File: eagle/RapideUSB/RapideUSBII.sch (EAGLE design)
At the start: 58 parts, among them J1 AVR_SPI_PRG_6PTH, Q1 12MHz, Y1 12-20MHz

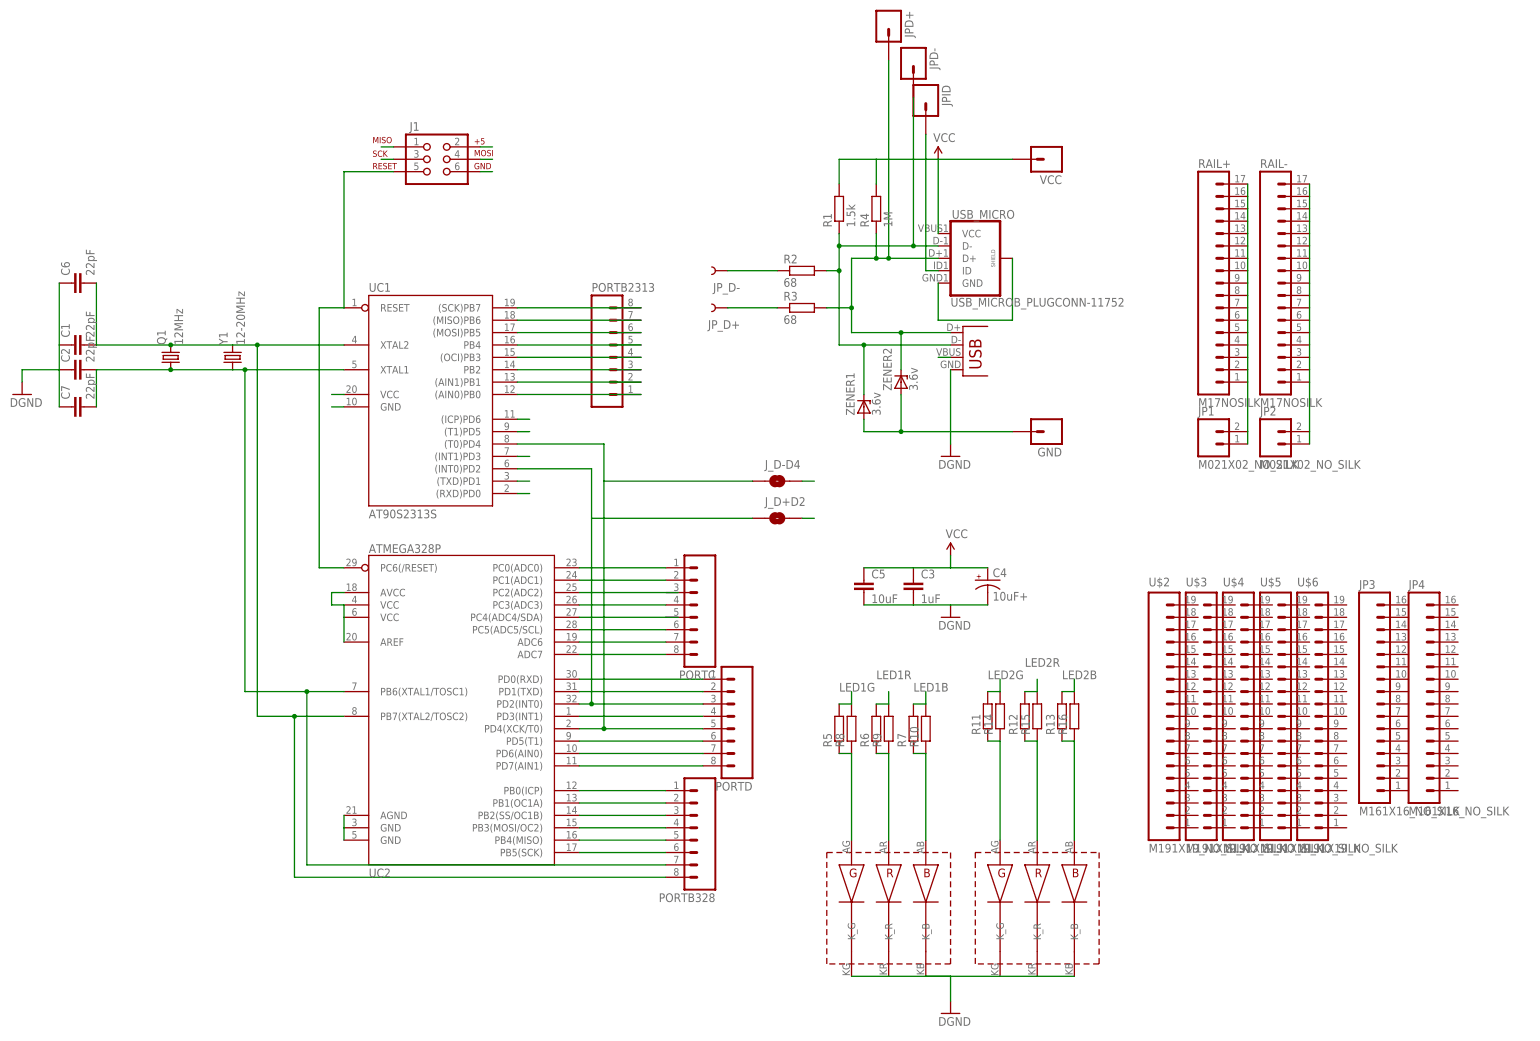
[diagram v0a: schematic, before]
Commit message: RapideUSBII : only 2313 before routing
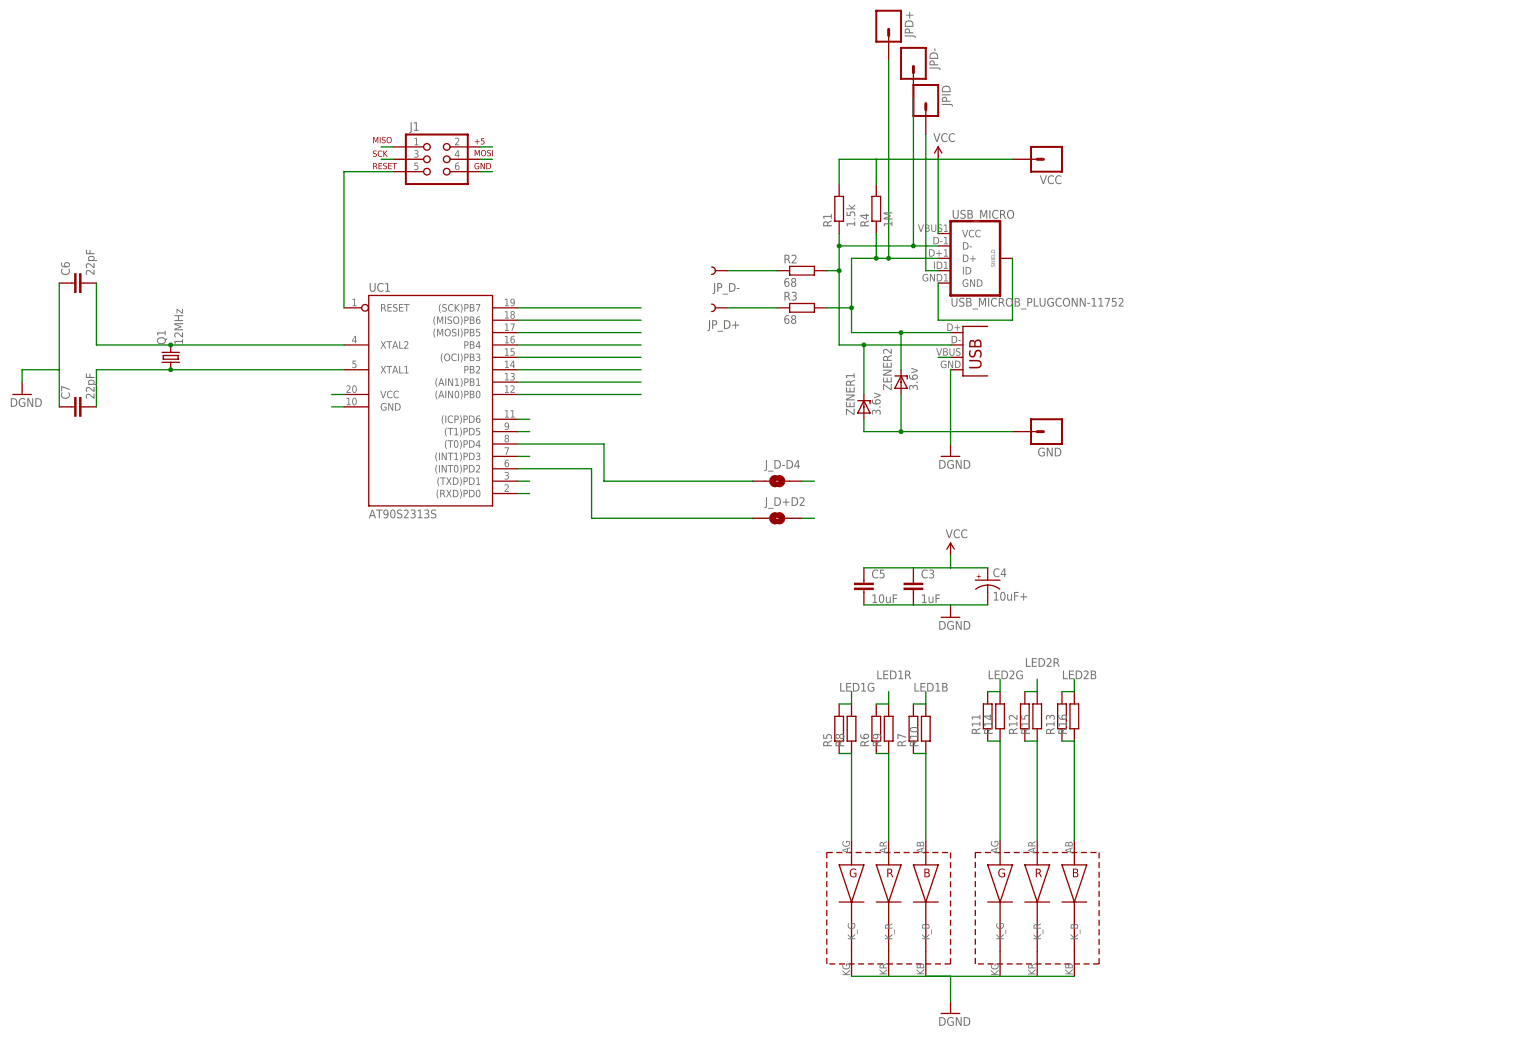
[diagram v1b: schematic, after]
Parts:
- removed C1, C2: 22pF, resistor:C-EU025-024X044
- removed JP1, JP2: M021X02_NO_SILK, SparkFun-Connectors:M021X02_NO_SILK
- removed JP3, JP4: M161X16_NO_SILK, SparkFun-Connectors:M161X16_NO_SILK
- removed PORTB2313, PORTB328, PORTC, PORTD: (no value), SparkFun-Connectors:M081X08
- removed RAIL+, RAIL-: M17NOSILK, SparkFun-Connectors:M17NOSILK
- removed U$2, U$3, U$4, U$5, U$6: M191X19_NO_SILK, SparkFun-Connectors:M191X19_NO_SILK
- removed UC2: ATMEGA328P, SparkFun-DigitalIC:ATMEGA328_SMT
- removed Y1: 12-20MHz, SparkFun-FreqCtrl:CRYSTALHC49UV
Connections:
- removed net B0: PORTB328.1, UC2.PB0(ICP)
- removed net B1: PORTB328.2, UC2.PB1(OC1A)
- removed net B2: PORTB328.3, UC2.PB2(SS/OC1B)
- removed net B6: C2.2, C7.2, PORTB328.7, Q1.1, UC1.XTAL1, UC2.PB6(XTAL1/TOSC1), Y1.1
- removed net B7: C1.2, C6.2, PORTB328.8, Q1.2, UC1.XTAL2, UC2.PB7(XTAL2/TOSC2), Y1.2
- removed net D7: PORTD.8, UC2.PD7(AIN1)
- removed net N$10: PORTC.6, UC2.PC5(ADC5/SCL)
- removed net N$11: PORTC.7, UC2.ADC6
- removed net N$12: PORTC.8, UC2.ADC7
- removed net N$16: PORTD.6, UC2.PD5(T1)
- removed net N$5: PORTC.1, UC2.PC0(ADC0)
- removed net N$6: PORTC.2, UC2.PC1(ADC1)
- removed net N$7: UC2.PC2(ADC2)
- removed net N$8: PORTC.4, UC2.PC3(ADC3)
- removed net N$9: PORTC.5, UC2.PC4(ADC4/SDA)
- new net N$22: C7.2, Q1.1, UC1.XTAL1
- new net N$23: C6.2, Q1.2, UC1.XTAL2
- net D0: no longer PORTD.1, UC2.PD0(RXD)
- net D1: no longer PORTD.2, UC2.PD1(TXD)
- net D2: no longer PORTD.3, UC2.PD2(INT0)
- net D3: no longer PORTD.4, UC2.PD3(INT1)
- net D4: no longer PORTD.5, UC2.PD4(XCK/T0)
- net D6: no longer PORTD.7, UC2.PD6(AIN0)
- net GND: no longer C1.1, C2.1, JP2.1, JP2.2, RAIL-.1, RAIL-.10, RAIL-.11, RAIL-.12, RAIL-.13, RAIL-.14, RAIL-.15, RAIL-.16, RAIL-.17, RAIL-.2, RAIL-.3, RAIL-.4, RAIL-.5, RAIL-.6, RAIL-.7, RAIL-.8, RAIL-.9, UC2.AGND, UC2.GND@1, UC2.GND@2
- net MISO: no longer PORTB2313.7, PORTB328.5, UC2.PB4(MISO)
- net MOSI: no longer PORTB2313.6, PORTB328.4, UC2.PB3(MOSI/OC2)
- net N$1: no longer PORTB2313.5
- net N$13: no longer PORTB2313.1
- net N$2: no longer PORTB2313.4
- net N$3: no longer PORTB2313.3
- net N$4: no longer PORTB2313.2
- net RESET: no longer UC2.PC6(/RESET)
- net SCK: no longer PORTB2313.8, PORTB328.6, UC2.PB5(SCK)
- net VCC: no longer JP1.1, JP1.2, RAIL+.1, RAIL+.10, RAIL+.11, RAIL+.12, RAIL+.13, RAIL+.14, RAIL+.15, RAIL+.16, RAIL+.17, RAIL+.2, RAIL+.3, RAIL+.4, RAIL+.5, RAIL+.6, RAIL+.7, RAIL+.8, RAIL+.9, UC2.AREF, UC2.AVCC, UC2.VCC@1, UC2.VCC@2

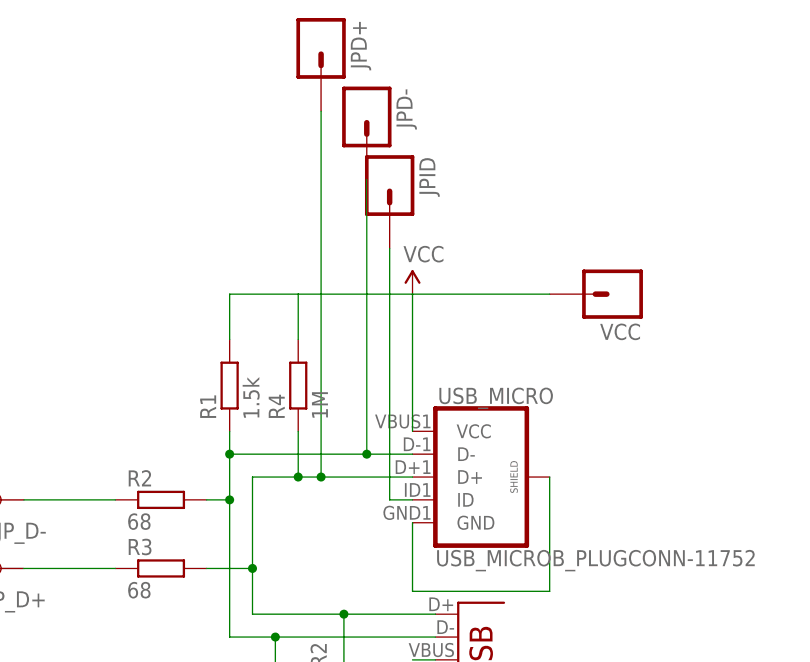
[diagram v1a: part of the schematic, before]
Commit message: Routed ok, need labelling
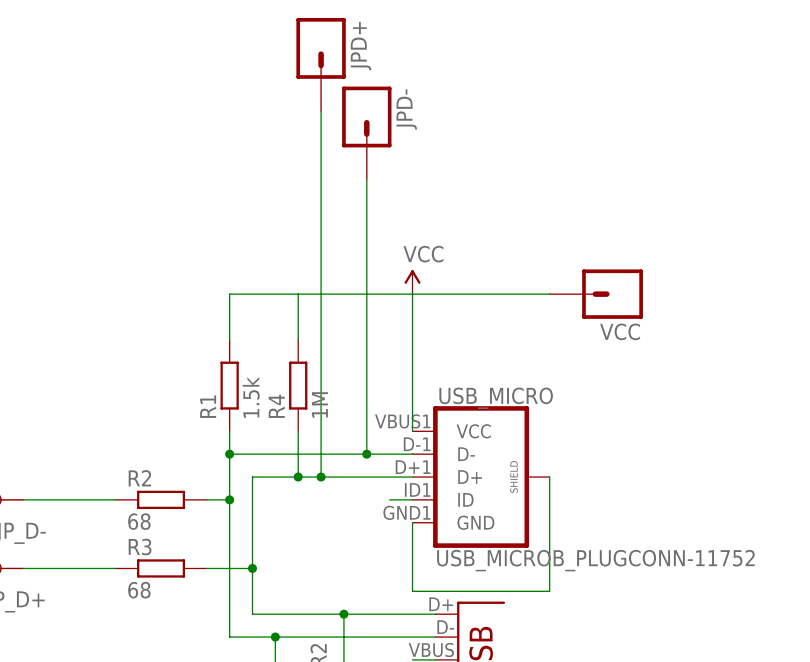
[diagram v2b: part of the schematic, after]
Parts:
- removed JPID: (no value), SparkFun-Connectors:M01PTH_NO_SILK_YES_STOP
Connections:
- removed net D5: UC1.(T1)PD5
- removed net D6: UC1.(ICP)PD6
- removed net N$13: UC1.(AIN0)PB0
- removed net N$2: UC1.(OCI)PB3
- removed net N$3: UC1.PB2
- removed net N$4: UC1.(AIN1)PB1
- net LED1B: now also UC1.(AIN0)PB0
- net LED1G: now also UC1.(ICP)PD6
- net LED1R: now also UC1.(T1)PD5
- net LED2B: now also UC1.(OCI)PB3
- net LED2G: now also UC1.PB2
- net LED2R: now also UC1.(AIN1)PB1
- net N$14: no longer JPID.1
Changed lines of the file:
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@@
 <part name="C7" library="SparkFun-Capacitors" deviceset="CAP" device="1206" value="22pF"/>
 <part name="Q1" library="crystal" deviceset="CRYSTAL" device="CTS406" value="12MHz"/>
-<part name="JPID" library="SparkFun-Connectors" deviceset="M01" device="PTH_NO_SILK_YES_STOP"/>
 <part name="LED1" library="kalshagar" deviceset="RGB-SMT-SQUARE" device="" technology="6X6MM"/>
 <part name="LED2" library="kalshagar" deviceset="RGB-SMT-SQUARE" device="5X5MM"/>
@@
 <instance part="C7" gate="G$1" x="-40.64" y="73.66" rot="R90"/>
 <instance part="Q1" gate="G$1" x="-22.86" y="83.82" rot="R90"/>
-<instance part="JPID" gate="G$1" x="132.08" y="137.16" rot="R270"/>
 <instance part="LED1" gate="G$1" x="124.46" y="-25.4"/>
 <instance part="LED2" gate="G$1" x="154.94" y="-25.4"/>
@@
 </segment>
 </net>
-<net name="D6" class="0">
-<segment>
-<pinref part="UC1" gate="G$1" pin="(ICP)PD6"/>
-<wire x1="48.26" y1="71.12" x2="50.8" y2="71.12" width="0.1524" layer="91"/>
-</segment>
-</net>
-<net name="D5" class="0">
-<segment>
-<pinref part="UC1" gate="G$1" pin="(T1)PD5"/>
-<wire x1="48.26" y1="68.58" x2="50.8" y2="68.58" width="0.1524" layer="91"/>
-</segment>
-</net>
 <net name="D3" class="0">
 <segment>
@@
 </segment>
 </net>
-<net name="N$2" class="0">
-<segment>
-<pinref part="UC1" gate="G$1" pin="(OCI)PB3"/>
-<wire x1="73.66" y1="83.82" x2="48.26" y2="83.82" width="0.1524" layer="91"/>
-</segment>
-</net>
-<net name="N$3" class="0">
-<segment>
-<pinref part="UC1" gate="G$1" pin="PB2"/>
-<wire x1="48.26" y1="81.28" x2="73.66" y2="81.28" width="0.1524" layer="91"/>
-</segment>
-</net>
-<net name="N$4" class="0">
-<segment>
-<pinref part="UC1" gate="G$1" pin="(AIN1)PB1"/>
-<wire x1="73.66" y1="78.74" x2="48.26" y2="78.74" width="0.1524" layer="91"/>
-</segment>
-</net>
-<net name="N$13" class="0">
-<segment>
-<pinref part="UC1" gate="G$1" pin="(AIN0)PB0"/>
-<wire x1="48.26" y1="76.2" x2="73.66" y2="76.2" width="0.1524" layer="91"/>
-</segment>
-</net>
 <net name="N$14" class="0">
 <segment>
-<pinref part="JPID" gate="G$1" pin="1"/>
-<wire x1="132.08" y1="129.54" x2="132.08" y2="101.6" width="0.1524" layer="91"/>
 <pinref part="USB_MICRO" gate="G$1" pin="ID"/>
 <wire x1="132.08" y1="101.6" x2="134.62" y2="101.6" width="0.1524" layer="91"/>
@@
 <label x="114.3" y="15.24" size="1.778" layer="95"/>
 </segment>
+<segment>
+<pinref part="UC1" gate="G$1" pin="(ICP)PD6"/>
+<wire x1="48.26" y1="71.12" x2="50.8" y2="71.12" width="0.1524" layer="91"/>
+</segment>
 </net>
 <net name="LED1R" class="0">
@@
 <label x="121.92" y="17.78" size="1.778" layer="95"/>
 </segment>
+<segment>
+<pinref part="UC1" gate="G$1" pin="(T1)PD5"/>
+<wire x1="48.26" y1="68.58" x2="50.8" y2="68.58" width="0.1524" layer="91"/>
+</segment>
 </net>
 <net name="LED1B" class="0">
@@
 <label x="129.54" y="15.24" size="1.778" layer="95"/>
 </segment>
+<segment>
+<pinref part="UC1" gate="G$1" pin="(AIN0)PB0"/>
+<wire x1="48.26" y1="76.2" x2="73.66" y2="76.2" width="0.1524" layer="91"/>
+</segment>
 </net>
 <net name="N$19" class="0">
@@
 <label x="144.78" y="17.78" size="1.778" layer="95"/>
 </segment>
+<segment>
+<pinref part="UC1" gate="G$1" pin="PB2"/>
+<wire x1="48.26" y1="81.28" x2="73.66" y2="81.28" width="0.1524" layer="91"/>
+</segment>
 </net>
 <net name="LED2R" class="0">
@@
 <label x="152.4" y="20.32" size="1.778" layer="95"/>
 </segment>
+<segment>
+<pinref part="UC1" gate="G$1" pin="(AIN1)PB1"/>
+<wire x1="73.66" y1="78.74" x2="48.26" y2="78.74" width="0.1524" layer="91"/>
+</segment>
 </net>
 <net name="LED2B" class="0">
@@
 <label x="160.02" y="17.78" size="1.778" layer="95"/>
 </segment>
-</net>
+<segment>
+<pinref part="UC1" gate="G$1" pin="(OCI)PB3"/>
+<wire x1="73.66" y1="83.82" x2="48.26" y2="83.82" width="0.1524" layer="91"/>
+</segment>
+</net>

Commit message: Before resuming working on RapiedUSBII, a quick commit of whatever I did.
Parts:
- added TP_ID: TEST-POINT3X5, SparkFun-Connectors:TEST-POINT3X5
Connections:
- net N$14: now also TP_ID.1

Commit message: Before routing
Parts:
- added H1: MOUNT-HOLE2.8, holes:MOUNT-HOLE2.8
- added J10: (no value), SparkFun-Connectors:CONN_08SMD-STRAIGHT-FEMALE
- added J2, J4, J5, J6, J7, J8: (no value), SparkFun-Connectors:CONN_08NO_SILK_FEMALE_PTH
- added J3: (no value), SparkFun-Connectors:CONN_08SMD-STRAIGHT-ALT-FEMALE
- added J9: (no value), SparkFun-Connectors:CONN_06NO_SILK_FEMALE_PTH
- Q1: device crystal:CRYSTALCTS406 -> SparkFun-Clocks:CRYSTALPTH-HC49UV
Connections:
- net D0: now also J10.8
- net D1: now also J10.7
- net D2: now also J10.6
- net D3: now also J10.5
- net D4: now also J10.4
- net GND: now also J9.1, J9.2, J9.3
- net LED1B: now also J3.8
- net LED1G: now also J10.2
- net LED1R: now also J10.3
- net LED2B: now also J3.5
- net LED2G: now also J3.6
- net LED2R: now also J3.7
- net MISO: now also J3.2
- net MOSI: now also J3.3
- net N$1: now also J3.4
- net SCK: now also J3.1
- net VCC: now also J9.4, J9.5, J9.6
